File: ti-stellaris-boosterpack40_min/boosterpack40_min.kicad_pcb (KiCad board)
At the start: 2 copper layers, 50.8 x 34.3 mm, 4 parts, among them J1 TI_BOOSTER_40_J1, J2 TI_BOOSTER_40_J2, J3 TI_BOOSTER_40_J3, J4 TI_BOOSTER_40_J4

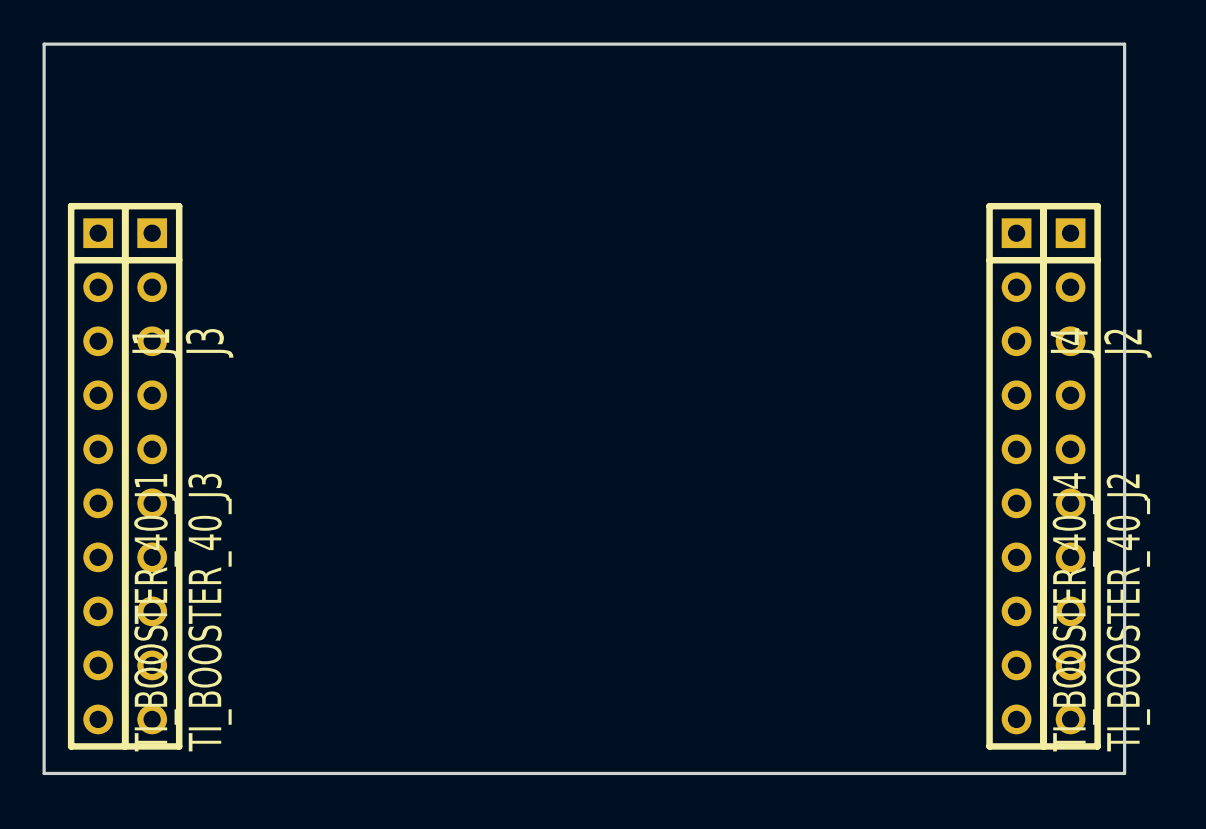
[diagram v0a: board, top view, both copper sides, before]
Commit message: Update ti stelaris and remove old duplicate that had no pcb file
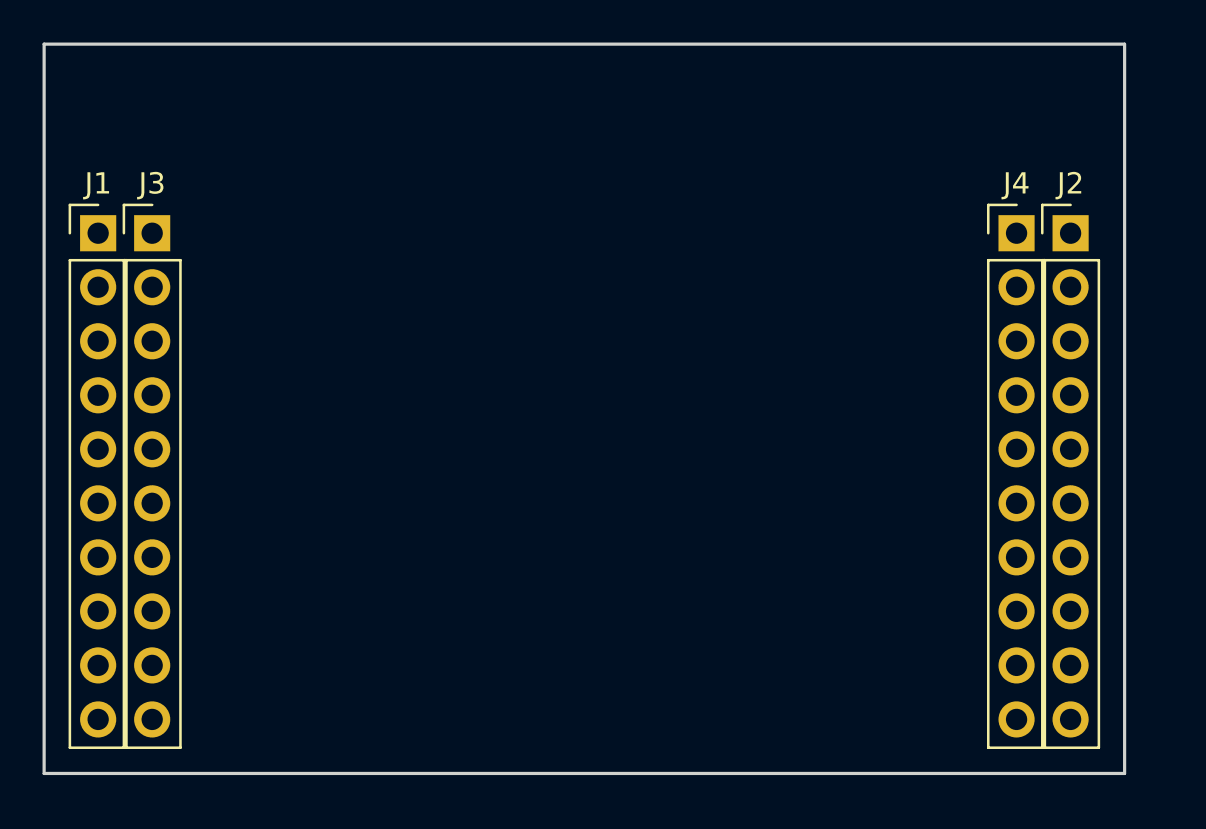
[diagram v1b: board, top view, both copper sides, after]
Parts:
- J1, J2, J3, J4: footprint Connect:SIL-10 -> Connector_PinHeader_2.54mm:PinHeader_1x10_P2.54mm_Vertical
- moved J1 11.4 mm to (185.4, 121.9), turned to 0 degrees
- moved J2 11.4 mm to (231.1, 121.9), turned to 0 degrees
- moved J3 11.4 mm to (188.0, 121.9), turned to 0 degrees
- moved J4 11.4 mm to (228.6, 121.9), turned to 0 degrees
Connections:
- J1 pad 1: (no net) -> VCC
- J1 pad 10: (no net) -> Net-(J1-Pad10)
- J1 pad 2: (no net) -> Net-(J1-Pad2)
- J1 pad 3: (no net) -> Net-(J1-Pad3)
- J1 pad 4: (no net) -> Net-(J1-Pad4)
- J1 pad 5: (no net) -> Net-(J1-Pad5)
- J1 pad 6: (no net) -> Net-(J1-Pad6)
- J1 pad 7: (no net) -> Net-(J1-Pad7)
- J1 pad 8: (no net) -> Net-(J1-Pad8)
- J1 pad 9: (no net) -> Net-(J1-Pad9)
- J2 pad 10: (no net) -> Net-(J2-Pad10)
- J2 pad 2: (no net) -> Net-(J2-Pad2)
- J2 pad 3: (no net) -> Net-(J2-Pad3)
- J2 pad 4: (no net) -> Net-(J2-Pad4)
- J2 pad 5: (no net) -> Net-(J2-Pad5)
- J2 pad 6: (no net) -> Net-(J2-Pad6)
- J2 pad 7: (no net) -> Net-(J2-Pad7)
- J2 pad 8: (no net) -> Net-(J2-Pad8)
- J2 pad 9: (no net) -> Net-(J2-Pad9)
- J3 pad 1: (no net) -> +5V
- J3 pad 10: (no net) -> Net-(J3-Pad10)
- J3 pad 3: (no net) -> Net-(J3-Pad3)
- J3 pad 4: (no net) -> Net-(J3-Pad4)
- J3 pad 5: (no net) -> Net-(J3-Pad5)
- J3 pad 6: (no net) -> Net-(J3-Pad6)
- J3 pad 7: (no net) -> Net-(J3-Pad7)
- J3 pad 8: (no net) -> Net-(J3-Pad8)
- J3 pad 9: (no net) -> Net-(J3-Pad9)
- J4 pad 1: (no net) -> Net-(J4-Pad1)
- J4 pad 10: (no net) -> Net-(J4-Pad10)
- J4 pad 2: (no net) -> Net-(J4-Pad2)
- J4 pad 3: (no net) -> Net-(J4-Pad3)
- J4 pad 4: (no net) -> Net-(J4-Pad4)
- J4 pad 5: (no net) -> Net-(J4-Pad5)
- J4 pad 6: (no net) -> Net-(J4-Pad6)
- J4 pad 7: (no net) -> Net-(J4-Pad7)
- J4 pad 8: (no net) -> Net-(J4-Pad8)
- J4 pad 9: (no net) -> Net-(J4-Pad9)
